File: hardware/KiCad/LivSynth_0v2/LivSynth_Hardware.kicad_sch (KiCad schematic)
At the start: 0 parts

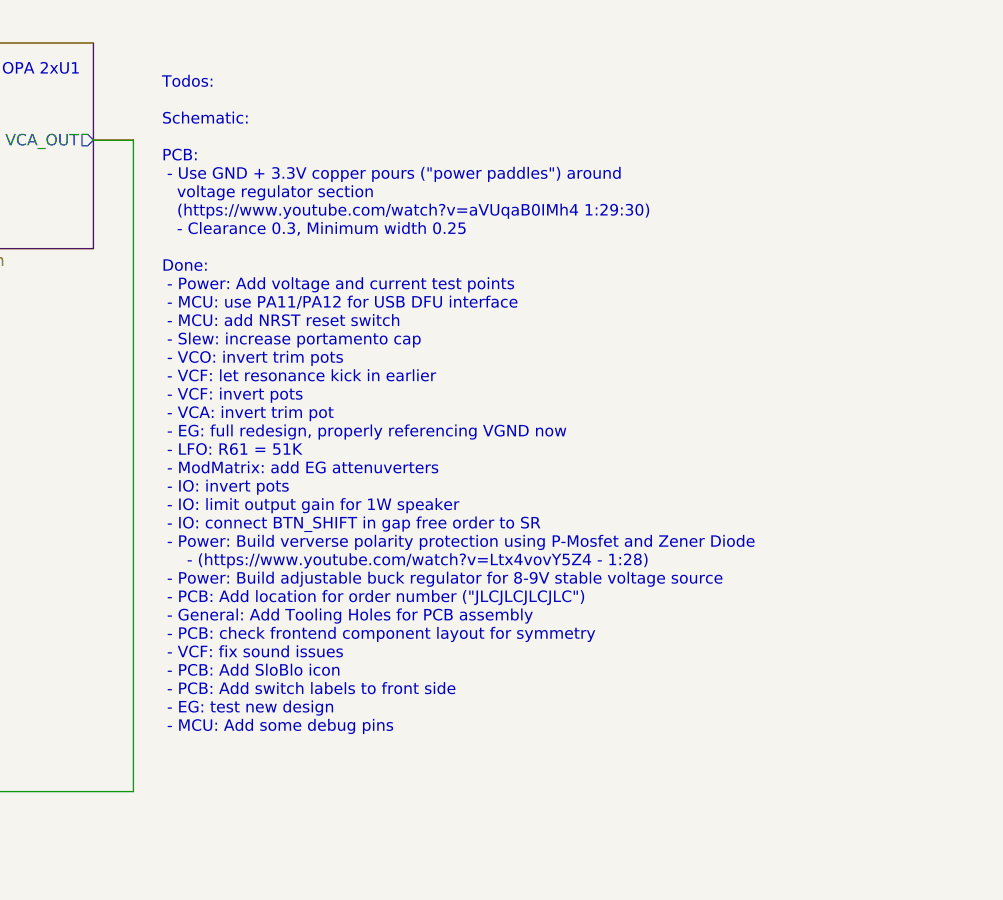
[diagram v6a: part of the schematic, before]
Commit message: LCSC component looked up
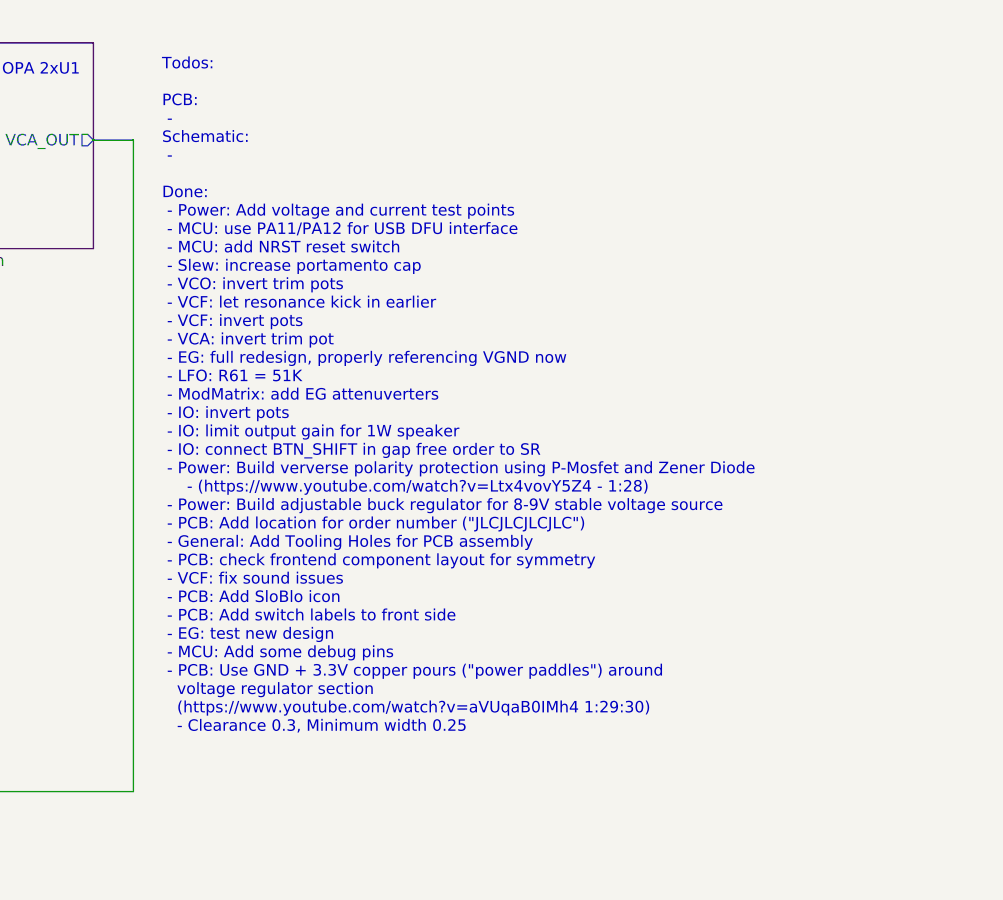
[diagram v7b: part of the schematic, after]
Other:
- note added: "Todos: PCB: - Schematic: - Done: - Power: Add voltage and current test points - MCU: use PA11/PA12 for USB DFU interface - MCU: add NRST reset switch - Slew: increase portamento cap - VCO: invert trim pots - VCF: let resonance kick in earlier - VCF: invert pots - VCA: invert trim pot - EG: full redesign, properly referencing VGND now - LFO: R61 = 51K - ModMatrix: add EG attenuverters - IO: invert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"
- note removed: "Todos: Schematic: PCB: - Use GND + 3.3V copper pours ("power paddles") around voltage regulator section (https://www.youtube.com/watch?v=aVUqaB0IMh4 1:29:30) - Clearance 0.3, Minimum width 0.25 Done: - Power: Add voltage and current test points - MCU: use PA11/PA12 for USB DFU interface - MCU: add NRST reset switch - Slew: increase portamento cap - VCO: invert trim pots - VCF: let resonance kick 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"
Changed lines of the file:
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@@
     (effects (font (size 1.27 1.27)) (justify left bottom))
   )
-  (text "Todos:\n\nSchematic:\n\nPCB:\n - Use GND + 3.3V copper pours (\"power paddles\") around\n   voltage regulator section\n   (https://www.youtube.com/watch?v=aVUqaB0IMh4 1:29:30)\n   - Clearance 0.3, Minimum width 0.25\n\nDone:\n - Power: Add voltage and current test points\n - MCU: use PA11/PA12 for USB DFU interface\n - MCU: add NRST reset switch\n - Slew: increase portamento cap\n - VCO: invert trim pots\n - VCF: let resonance kick in earlier\n - VCF: invert pots\n - VCA: invert trim pot\n - EG: full redesign, properly referencing VGND now\n - LFO: R61 = 51K\n - ModMatrix: add EG attenuverters\n - IO: invert pots\n - IO: limit output gain for 1W speaker\n - IO: connect BTN_SHIFT in gap free order to SR\n - Power: Build ververse polarity protection using P-Mosfet and Zener Diode\n     - (https://www.youtube.com/watch?v=Ltx4vovY5Z4 - 1:28)\n - Power: Build adjustable buck regulator for 8-9V stable voltage source\n - PCB: Add location for order number (\"JLCJLCJLCJLC\")\n - General: Add Tooling Holes for PCB assembly\n - PCB: check frontend component layout for symmetry\n - VCF: fix sound issues\n - PCB: Add SloBlo icon\n - PCB: Add switch labels to front side\n - EG: test new design\n - MCU: Add some debug pins"
+  (text "Todos:\n\nPCB:\n - \nSchematic:\n - \n\nDone:\n - Power: Add voltage and current test points\n - MCU: use PA11/PA12 for USB DFU interface\n - MCU: add NRST reset switch\n - Slew: increase portamento cap\n - VCO: invert trim pots\n - VCF: let resonance kick in earlier\n - VCF: invert pots\n - VCA: invert trim pot\n - EG: full redesign, properly referencing VGND now\n - LFO: R61 = 51K\n - ModMatrix: add EG attenuverters\n - IO: invert pots\n - IO: limit output gain for 1W speaker\n - IO: connect BTN_SHIFT in gap free order to SR\n - Power: Build ververse polarity protection using P-Mosfet and Zener Diode\n     - (https://www.youtube.com/watch?v=Ltx4vovY5Z4 - 1:28)\n - Power: Build adjustable buck regulator for 8-9V stable voltage source\n - PCB: Add location for order number (\"JLCJLCJLCJLC\")\n - General: Add Tooling Holes for PCB assembly\n - PCB: check frontend component layout for symmetry\n - VCF: fix sound issues\n - PCB: Add SloBlo icon\n - PCB: Add switch labels to front side\n - EG: test new design\n - MCU: Add some debug pins\n - PCB: Use GND + 3.3V copper pours (\"power paddles\") around\n   voltage regulator section\n   (https://www.youtube.com/watch?v=aVUqaB0IMh4 1:29:30)\n   - Clearance 0.3, Minimum width 0.25"
     (at 212.09 99.695 0)
     (effects (font (size 1.27 1.27)) (justify left bottom))
@@
     )
     (path "/9b71f1c4-49e8-4b79-9df9-1d6c393fba92/1fbb261a-fa29-467e-9429-2a5861057524"
-      (reference "C40") (unit 1) (value "1u") (footprint "Capacitor_THT:C_Rect_L7.2mm_W2.5mm_P5.00mm_FKS2_FKP2_MKS2_MKP2")
+      (reference "C40") (unit 1) (value "1u") (footprint "Capacitor_THT:C_Rect_L7.2mm_W5.5mm_P5.00mm_FKS2_FKP2_MKS2_MKP2")
     )
     (path "/429bbaa1-cd91-4d0a-bb36-7b198f9f0350/0156eb88-117a-4faf-a1df-a63c12c3548c"
@@
     )
     (path "/429bbaa1-cd91-4d0a-bb36-7b198f9f0350/bd2b7833-3c88-4421-ae0e-a9a4b29f10e8"
-      (reference "C208") (unit 1) (value "100n") (footprint "Capacitor_THT:C_Rect_L7.2mm_W2.5mm_P5.00mm_FKS2_FKP2_MKS2_MKP2")
+      (reference "C208") (unit 1) (value "100n") (footprint "Capacitor_SMD:C_0402_1005Metric_Pad0.74x0.62mm_HandSolder")
     )
     (path "/429bbaa1-cd91-4d0a-bb36-7b198f9f0350/679d45a9-4fdd-4e96-9e76-e0eac0c82126"
@@
     )
     (path "/2b2b077d-6195-4e26-8c81-d35bbd189e15/5aaacbb9-88fb-43a3-831a-2f23f0fa8f62"
-      (reference "R71") (unit 1) (value "100") (footprint "Resistor_THT:R_Axial_DIN0207_L6.3mm_D2.5mm_P7.62mm_Horizontal")
+      (reference "R71") (unit 1) (value "${VCF_Rsmall_Value}") (footprint "Resistor_THT:R_Axial_DIN0207_L6.3mm_D2.5mm_P7.62mm_Horizontal")
     )
     (path "/7424e654-f944-437f-a698-e5c80517338a/baff0e71-7627-4382-9811-c3cb28e77f6f"
@@
     )
     (path "/2b2b077d-6195-4e26-8c81-d35bbd189e15/cfff1b88-065a-4ed6-bc82-13879cd02210"
-      (reference "R76") (unit 1) (value "100") (footprint "Resistor_THT:R_Axial_DIN0207_L6.3mm_D2.5mm_P7.62mm_Horizontal")
+      (reference "R76") (unit 1) (value "${VCF_Rsmall_Value}") (footprint "Resistor_THT:R_Axial_DIN0207_L6.3mm_D2.5mm_P7.62mm_Horizontal")
     )
     (path "/2b2b077d-6195-4e26-8c81-d35bbd189e15/38e5e28b-df11-4878-9e47-3fa58f23e72e"
@@
     )
     (path "/2b2b077d-6195-4e26-8c81-d35bbd189e15/83b4dcb1-a701-49ab-826f-3fda44becbd6"
-      (reference "R88") (unit 1) (value "100") (footprint "Resistor_THT:R_Axial_DIN0207_L6.3mm_D2.5mm_P7.62mm_Horizontal")
+      (reference "R88") (unit 1) (value "${VCF_Rsmall_Value}") (footprint "Resistor_THT:R_Axial_DIN0207_L6.3mm_D2.5mm_P7.62mm_Horizontal")
     )
     (path "/2b2b077d-6195-4e26-8c81-d35bbd189e15/fc3be260-52f8-420b-b665-46ae48299b5f"
@@
     )
     (path "/2b2b077d-6195-4e26-8c81-d35bbd189e15/5d649fb5-ecd1-44ac-be03-312121ece057"
-      (reference "R91") (unit 1) (value "100") (footprint "Resistor_THT:R_Axial_DIN0207_L6.3mm_D2.5mm_P7.62mm_Horizontal")
+      (reference "R91") (unit 1) (value "${VCF_Rsmall_Value}") (footprint "Resistor_THT:R_Axial_DIN0207_L6.3mm_D2.5mm_P7.62mm_Horizontal")
     )
     (path "/2b2b077d-6195-4e26-8c81-d35bbd189e15/8d1ac0c1-61b0-4707-abfd-c1a9b9bf36c9"
